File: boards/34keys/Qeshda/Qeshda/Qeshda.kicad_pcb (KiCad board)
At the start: 2 copper layers, 230.5 x 102.4 mm, 75 parts, among them J1 Conn_01x08_Female, SW1 SW_Push, SW10 SW_Push, SW11 SW_Push, SW12 SW_Push, SW13 SW_Push, SW14 SW_Push, SW15 SW_Push, SW16 SW_Push, SW17 SW_Push, SW18 SW_Push, SW19 SW_Push, SW2 SW_Push, SW20 SW_Push, SW21 SW_Push, SW22 SW_Push, SW23 SW_Push, SW24 SW_Push, SW25 SW_SPDT, SW26 Rotary_Encoder_Switch, SW27 SW_Push, SW28 SW_Push, SW29 SW_Push, SW3 SW_Push, SW30 SW_Push, SW31 SW_Push, SW32 SW_Push, SW34 SW_Push, SW37 SW_Push, SW38 SW_Push, SW39 SW_Push, SW4 SW_Push, SW40 SW_Push, SW5 SW_Push, SW6 SW_Push, SW7 SW_Push, SW8 SW_Push, SW9 SW_Push, U1 nice_nano

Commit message: More space for encoder in Qeschda
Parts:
- added SW33: SW_SPDT, Button_Switch_SMD:SW_SPDT_PCM12, B.Cu at (153.8, 117.0)
- moved SW34 9.95 mm to (169.1, 90.0), turned to 90 degrees
- moved D25 5.00 mm to (165.5, 101.7)
- moved Display1 5.00 mm to (153.8, 66.5)
- moved SW26 5.00 mm to (154.0, 99.2)
- moved U1 5.00 mm to (153.9, 63.6)
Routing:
- net col_5: track 180.6 -> 203.0 mm, vias 3 -> 4
- net row_4: track 123.7 -> 142.7 mm, vias 4 -> 5
- net col_4: track 124.0 -> 142.0 mm, vias 3 -> 4
- net GND: track 18.6 -> 1.67 mm, vias 30 -> 32
- net col_0: track 200.7 -> 216.6 mm, vias 2 -> 3
- net RESET: track 63.7 -> 52.1 mm
- net EncR: track 67.6 -> 57.5 mm
- net RAW: track 75.3 -> 82.6 mm
- net col_7: track 166.1 -> 171.3 mm
- net col_3: track 145.5 -> 150.5 mm, vias 2 -> 4
- net col_2: track 145.9 -> 150.4 mm, vias 3 -> 4
- net EncL: track 65.8 -> 70.1 mm
- net row_2: track 254.5 -> 258.2 mm
- net row_1: track 272.5 -> 268.8 mm, vias 12 -> 10
- net bat+: track 44.0 -> 46.1 mm, vias 1 -> 2
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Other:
- outline, holes or cut-outs redrawn

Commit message: Qeshda update
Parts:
- added ?: , , F.Cu at (244.3, 42.4)
- added ?: , , F.Cu at (135.6, 47.2)
- added ?: , , F.Cu at (248.2, 76.2)
- added ?: , , F.Cu at (169.4, 47.2)
- added ?: , , F.Cu at (174.5, 102.4)
- added ?: , , F.Cu at (134.4, 102.4)
- added ?: , , F.Cu at (64.0, 42.4)
- added ?: , , F.Cu at (58.9, 76.2)
- moved D23 2.89 mm to (244.1, 76.5)
- moved D9 2.28 mm to (57.1, 70.9)
- moved Display1 1.00 mm to (153.8, 67.5)
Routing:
- net GND: track 1.67 -> 20.8 mm, vias 32 -> 45
- net row_0: track 294.8 -> 305.9 mm
- net col_3: track 150.5 -> 154.2 mm
- net col_0: track 216.6 -> 213.5 mm
- net col_4: track 142.0 -> 143.8 mm
- net MOSI: track 36.0 -> 37.7 mm
- net SCK: track 30.9 -> 32.5 mm
- net row_1: track 268.8 -> 270.3 mm
- net NVCS: track 35.9 -> 36.9 mm
- net 3V3: track 33.1 -> 34.1 mm
- net Net-(D23-A): track 7.76 -> 6.92 mm
- net Net-(D9-A): track 7.38 -> 6.56 mm
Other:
- outline, holes or cut-outs redrawn

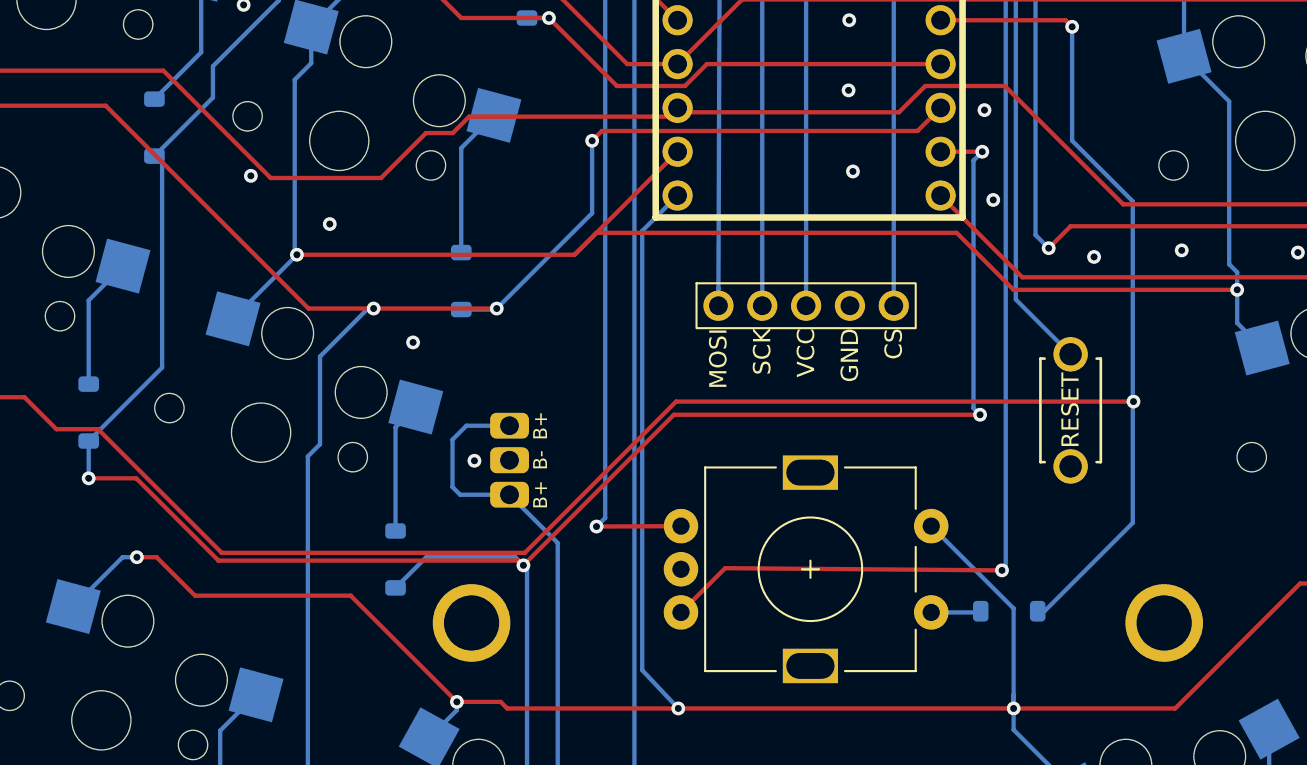
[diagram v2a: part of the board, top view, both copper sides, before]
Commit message: Qeshda move JST connector to have more space
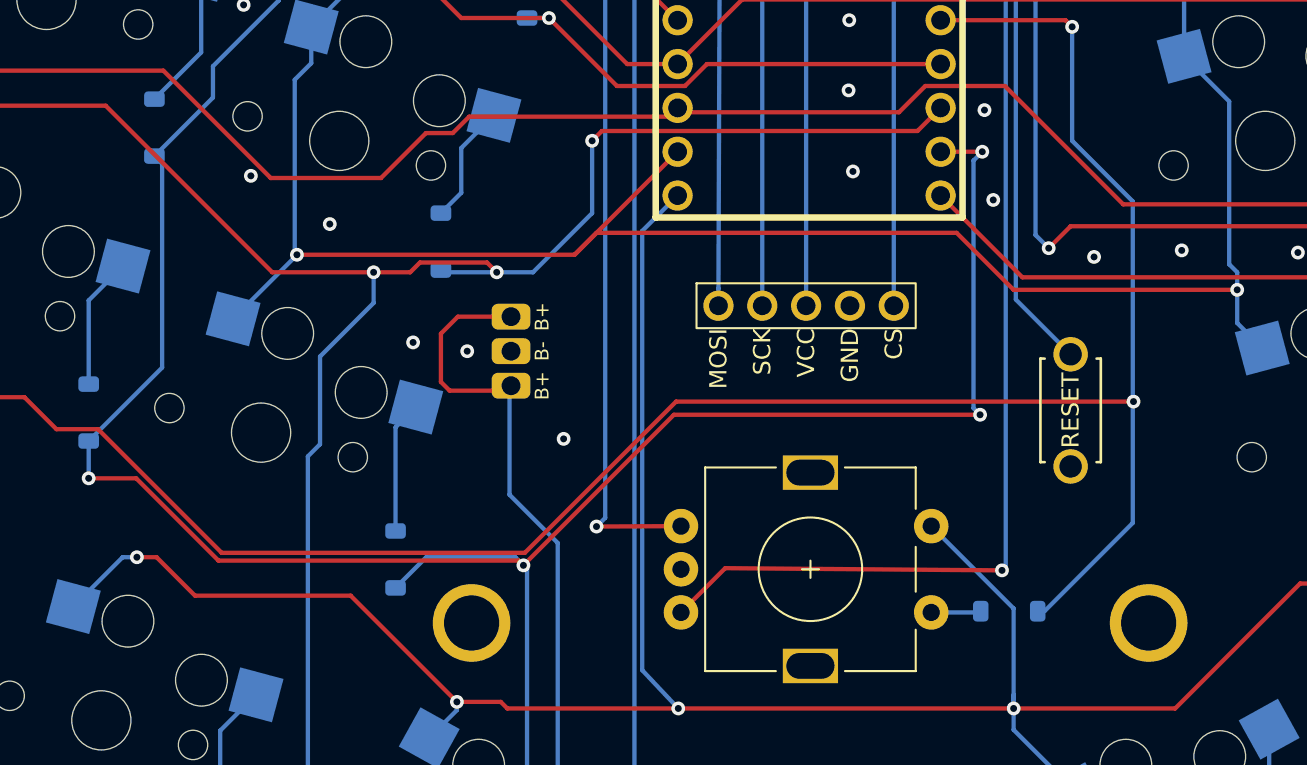
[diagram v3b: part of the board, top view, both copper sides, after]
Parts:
- moved J1 6.32 mm to (136.7, 86.6)
- moved D27 2.57 mm to (132.6, 80.3)
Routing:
- net bat+: track 46.3 -> 54.4 mm
- net col_2: track 150.4 -> 152.2 mm
- net Net-(D27-A): track 8.74 -> 6.94 mm
- net GND: vias 45 -> 46
